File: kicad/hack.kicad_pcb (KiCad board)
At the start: 2 copper layers, 33.9 x 24.1 mm, 34 parts, among them P1 USB_micro, P2 CONN_01X13, P3 CONN_01X13, P4 CONN_01X01, U1 MIC5528, U2 STF202, U3 ATSAMD21E, X1 ABS07

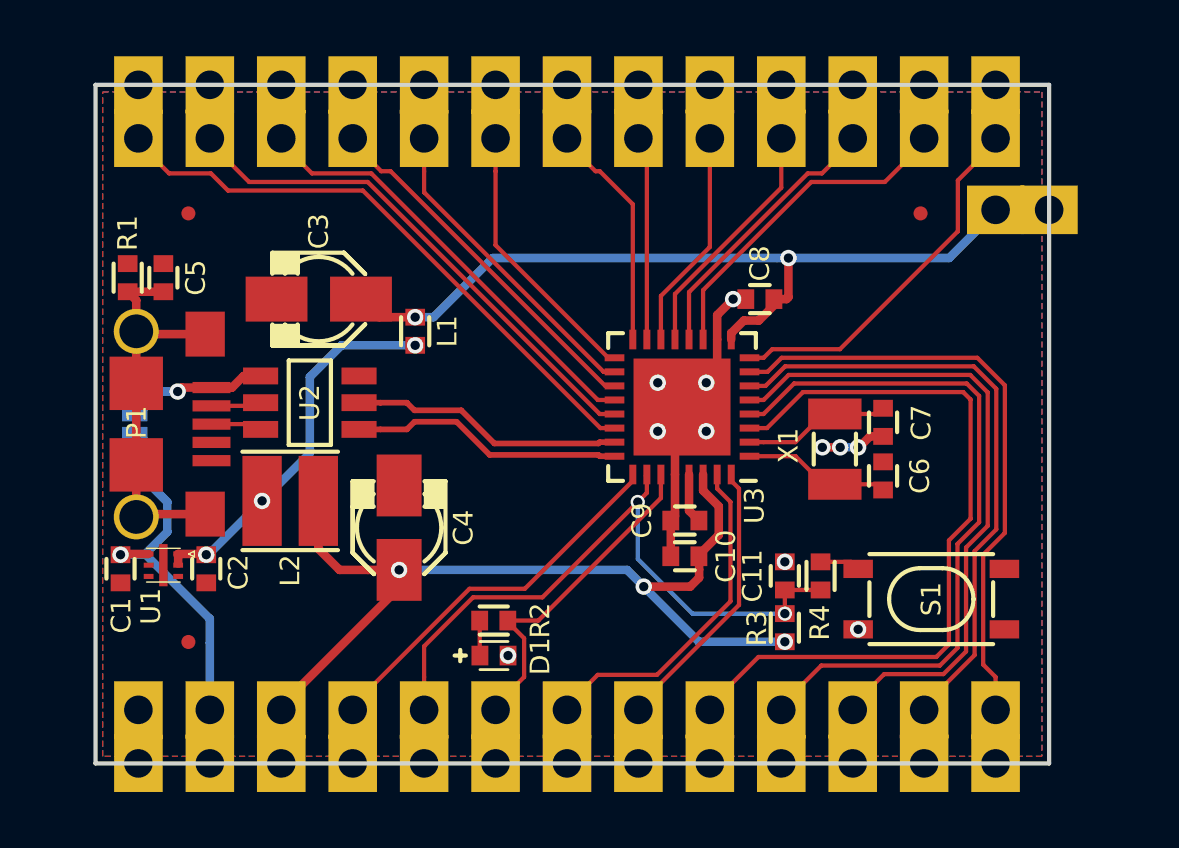
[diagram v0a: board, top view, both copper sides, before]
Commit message: Added VBUS pin, GND pin near VDDANA
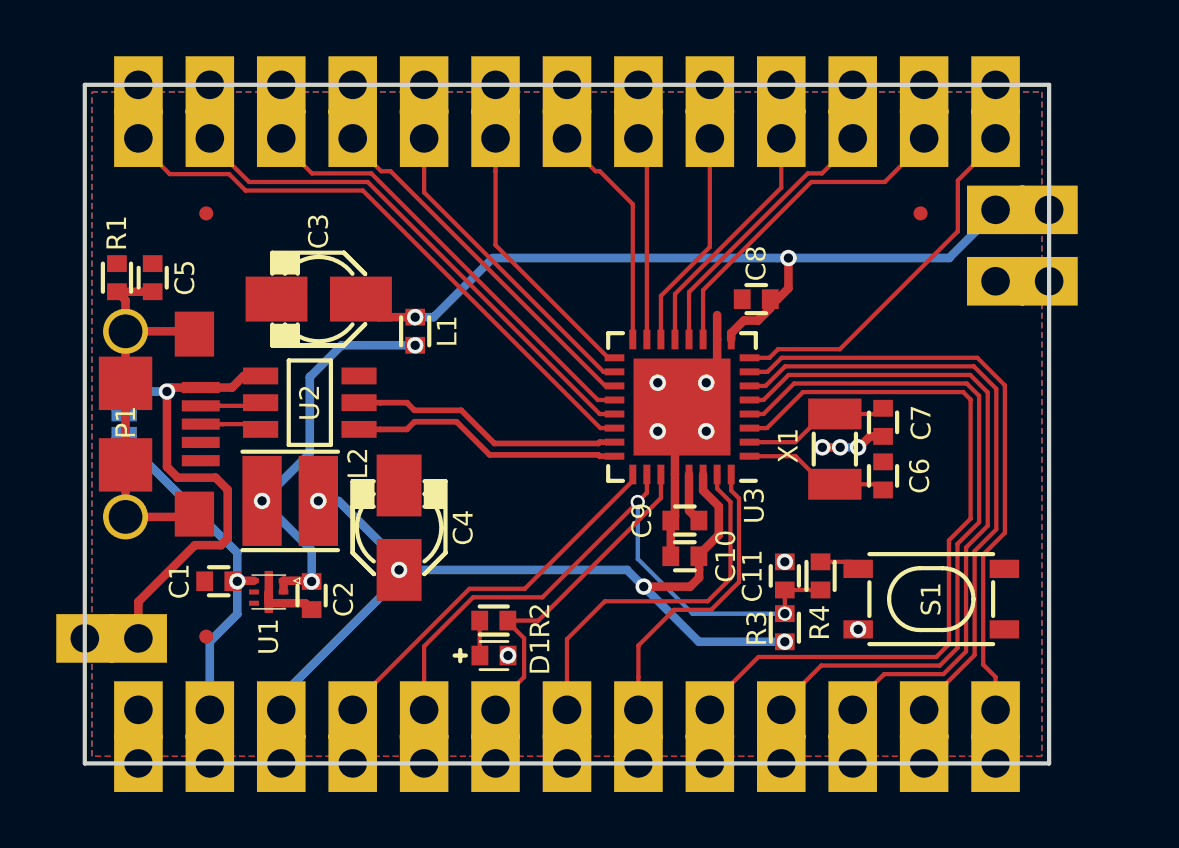
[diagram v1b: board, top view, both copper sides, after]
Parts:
- added P5: CONN_01X01, hack-footprints:Pin_Castellated_1x01, F.Cu at (154.9, 94.0)
- added P6: CONN_01X01, hack-footprints:Pin_Castellated_1x01, F.Cu at (185.4, 81.3)
- moved C2 3.87 mm to (161.1, 92.5)
- moved U1 3.87 mm to (159.6, 92.3)
- moved C1 3.52 mm to (157.8, 91.9), turned to 180 degrees
- moved FID1 0.66 mm to (157.4, 93.9)
- moved FID2 0.64 mm to (157.4, 78.9)
- moved LOGO1 0.63 mm to (179.7, 88.9)
- moved LOGO2 0.63 mm to (160.7, 88.9)
- moved LOGO3 0.63 mm to (170.2, 82.5)
- moved C5 0.38 mm to (155.4, 81.2)
- moved JP1 0.38 mm to (154.4, 86.4)
- moved P1 0.38 mm to (154.5, 86.4)
- moved R1 0.38 mm to (154.2, 81.2)
- moved C8 0.13 mm to (176.9, 81.9)
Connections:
- P1 pad 4: (no net) -> Net-(P1-Pad4)
- S1 pad 2: (no net) -> Net-(S1-Pad2)
- S1 pad 4: (no net) -> Net-(S1-Pad4)
- U1 pad 4: (no net) -> Net-(U1-Pad4)
- U1 pad 5: (no net) -> Net-(U1-Pad5)
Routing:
- net VBUS: track 4.95 -> 19.6 mm
- net GND: track 11.5 -> 15.2 mm, vias 11 -> 10
- net PA31/SWDIO: track 12.1 -> 13.2 mm
- net PA30/SWCLK: track 14.1 -> 15.2 mm
- net VDD: track 13.5 -> 14.3 mm
- net Net-(P1-Pad3): track 1.83 -> 2.63 mm
- net Net-(P1-Pad2): track 1.79 -> 2.50 mm
- net VLDO: track 15.2 -> 14.7 mm
- net /shield: track 14.4 -> 14.9 mm
- net VDDF: vias 3 -> 4
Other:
- board size 33.9 x 24.1 mm -> 34.3 x 24.1 mm
- board text added: "GND VDDA A5"
- board text added: "VBUS"
- board text removed: "VDDA/A5"

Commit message: Reducing board size (w.i.p.)
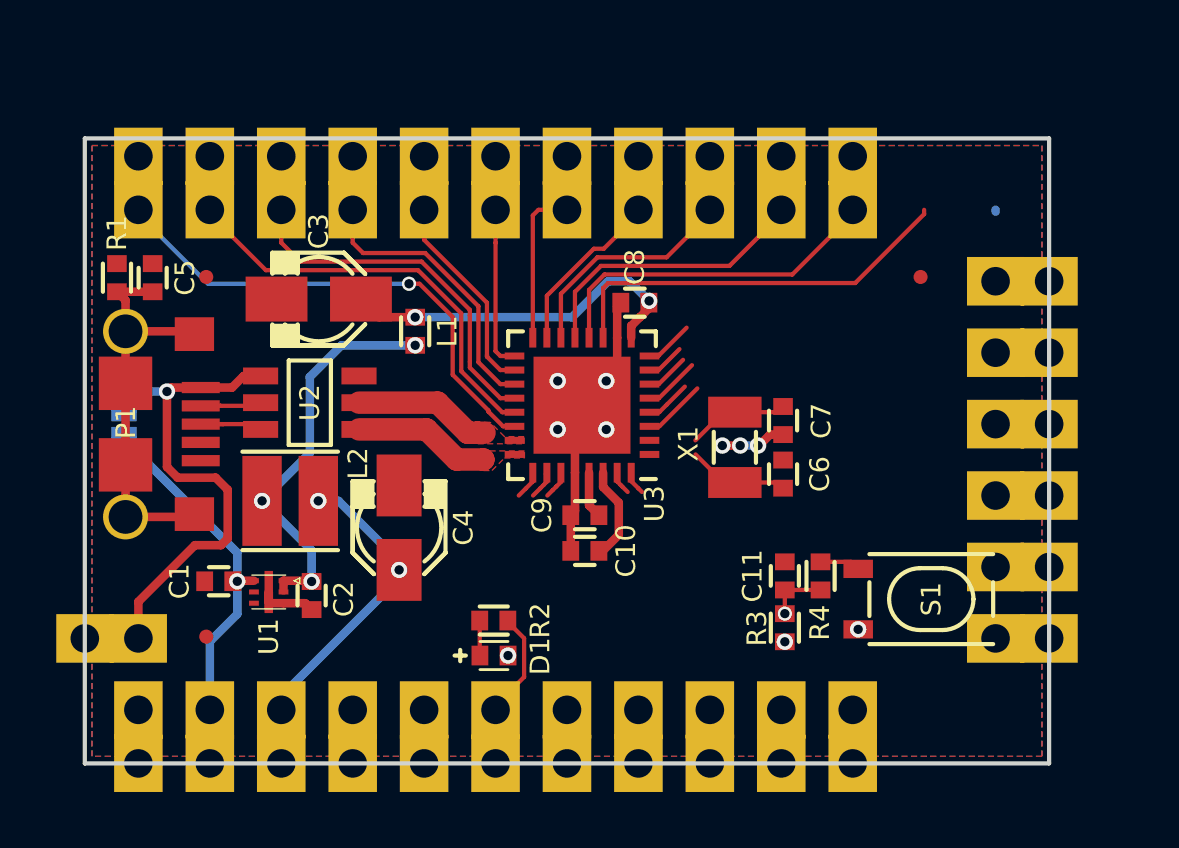
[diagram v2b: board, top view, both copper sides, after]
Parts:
- removed P6: CONN_01X01, hack-footprints:Pin_Castellated_1x01
- P2, P3: value CONN_01X13 -> CONN_01X11; footprint hack-footprints:Pin_Castellated_1x13 -> hack-footprints:Pin_Castellated_1x11
- P4: value CONN_01X01 -> CONN_01X06; footprint hack-footprints:Pin_Castellated_1x01 -> hack-footprints:Pin_Castellated_1x06; moved to F.Cu
- moved P3 30.5 mm to (154.9, 76.8), turned to 270 degrees
- moved C8 4.32 mm to (172.6, 82.0)
- moved C10 3.56 mm to (170.8, 90.9)
- moved C9 3.56 mm to (170.8, 89.6)
- moved C6 3.56 mm to (177.9, 88.1)
- moved C7 3.56 mm to (177.9, 86.2)
- moved U3 3.56 mm to (170.7, 85.7)
- moved X1 3.56 mm to (176.1, 87.2)
- moved P4 2.54 mm to (185.4, 81.3)
- moved FID3 2.41 mm to (182.8, 81.3)
- moved FID2 2.26 mm to (157.4, 81.1)
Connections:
- P3 pad 1: PA07/A5 -> PA23/11
- P3 pad 10: PA18/8 -> PA10/2
- P3 pad 11: PA19/9 -> PA09/1
- P3 pad 2: PA08/0 -> PA22/10
- P3 pad 3: PA09/1 -> PA19/9
- P3 pad 4: PA10/2 -> PA18/8
- P3 pad 5: PA11/3 -> PA17/7
- P3 pad 6: PA14/4 -> PA16/6
- P3 pad 8: PA16/6 -> PA14/4
- P3 pad 9: PA17/7 -> PA11/3
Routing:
- net PA02/A0: track 29.0 -> 4.16 mm
- net PA03/A1: track 27.3 -> 3.54 mm
- net PA06/A4: track 23.6 -> 1.37 mm
- net PA05/A3: track 23.8 -> 1.55 mm
- net PA04/A2: track 25.5 -> 3.90 mm
- net !RESET: track 25.4 -> 5.24 mm, vias 2 -> 1
- net VDDANA: track 30.5 -> 12.8 mm
- net VDDF: track 34.5 -> 16.9 mm, vias 4 -> 3
- net PA07/A5: track 15.0 -> 1.74 mm
- net PA27/12: track 15.7 -> 3.23 mm
- net PA30/SWCLK: track 15.2 -> 2.90 mm
- net PA31/SWDIO: track 13.2 -> 3.34 mm
- net PA28/13: track 14.0 -> 6.91 mm
- net PA17/7: track 13.4 -> 7.39 mm
- net PA16/6: track 11.7 -> 5.77 mm
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- added copper zone on F.Cu, net USB-D+
- added copper zone on F.Cu, net USB-D-
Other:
- board size 34.3 x 24.1 mm -> 34.3 x 22.2 mm
- net class USB: clearance 0.1524 -> 0.1523; trace_width 0.254 -> 0.8

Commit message: Reduced overall board size
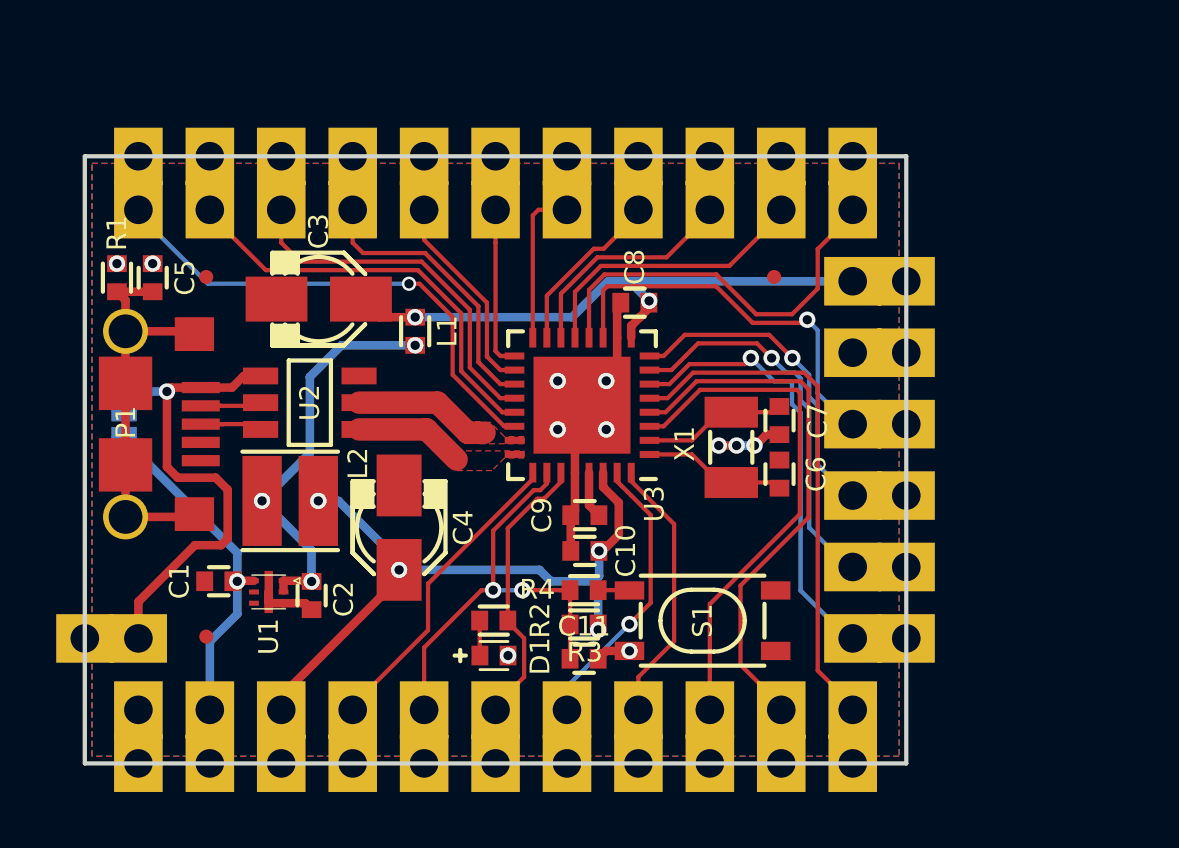
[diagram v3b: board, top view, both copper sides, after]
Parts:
- LOGO3: footprint hack-footprints:HACK-LOGO -> hack-footprints:HACK-small
- moved R4 8.42 mm to (170.8, 92.3), turned to 0 degrees
- moved S1 8.17 mm to (175.0, 93.3)
- moved C11 7.72 mm to (170.8, 94.7), turned to 0 degrees
- moved R3 7.14 mm to (170.8, 93.5), turned to 0 degrees
- moved FID3 5.21 mm to (177.5, 81.3)
- moved LOGO1 5.12 mm to (174.6, 88.3)
- moved P4 5.08 mm to (180.3, 81.3)
- moved LOGO3 3.24 mm to (167.0, 83.2)
- moved LOGO2 1.42 mm to (159.4, 88.3)
- moved X1 0.13 mm to (176.0, 87.2)
- moved C6 0.13 mm to (177.7, 88.1)
- moved C7 0.13 mm to (177.7, 86.2)
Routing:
- net PA03/A1: track 3.54 -> 21.5 mm
- net PA04/A2: track 3.90 -> 20.8 mm
- net PA02/A0: track 4.16 -> 20.6 mm
- net PA05/A3: track 1.55 -> 17.8 mm, vias 0 -> 1
- net PA06/A4: track 1.37 -> 15.7 mm, vias 0 -> 1
- net !RESET: track 5.24 -> 17.8 mm, vias 1 -> 2
- net PA07/A5: track 1.74 -> 13.5 mm, vias 0 -> 1
- net PA27/12: track 3.23 -> 13.1 mm
- net VDDF: track 16.9 -> 26.8 mm, vias 3 -> 4
- net VDDANA: track 12.8 -> 22.7 mm
- net PA30/SWCLK: track 2.90 -> 12.1 mm, vias 0 -> 1
- net PA31/SWDIO: track 3.34 -> 12.1 mm
- net PA28/13: track 6.91 -> 12.1 mm
- net PA09/1: track 12.3 -> 16.2 mm
- net GND: track 13.6 -> 16.7 mm, vias 9 -> 11
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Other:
- board size 34.3 x 22.2 mm -> 29.2 x 21.6 mm
- net class Default: via_dia 0.508 -> 0.5842
- board text added: "A5"
- board text added: "VDDA"
- board text removed: "GND VDDA A5"
